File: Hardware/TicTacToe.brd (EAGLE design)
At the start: 111.7 x 101.3 mm, 37 parts, among them J1 ARDUINO_R3_SHIELD

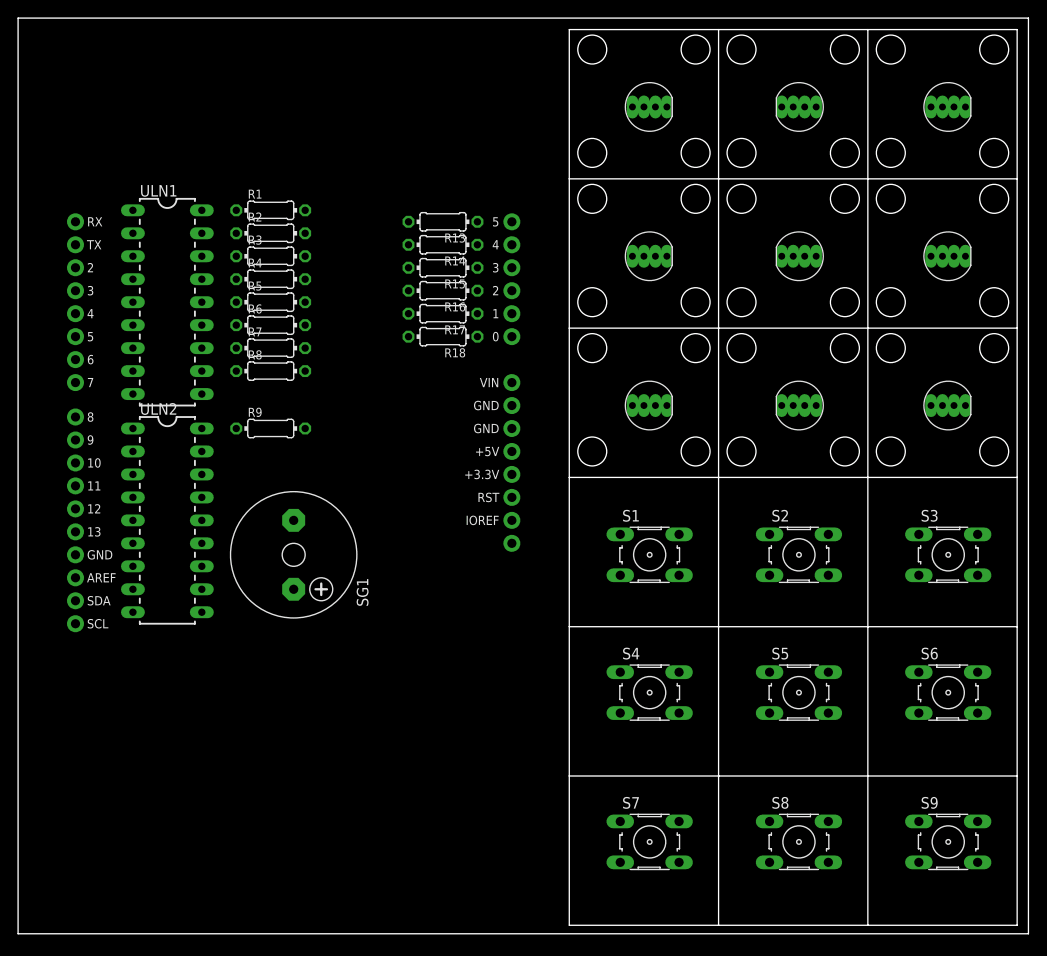
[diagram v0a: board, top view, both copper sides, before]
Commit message: Pequeño enrutado del pcb board
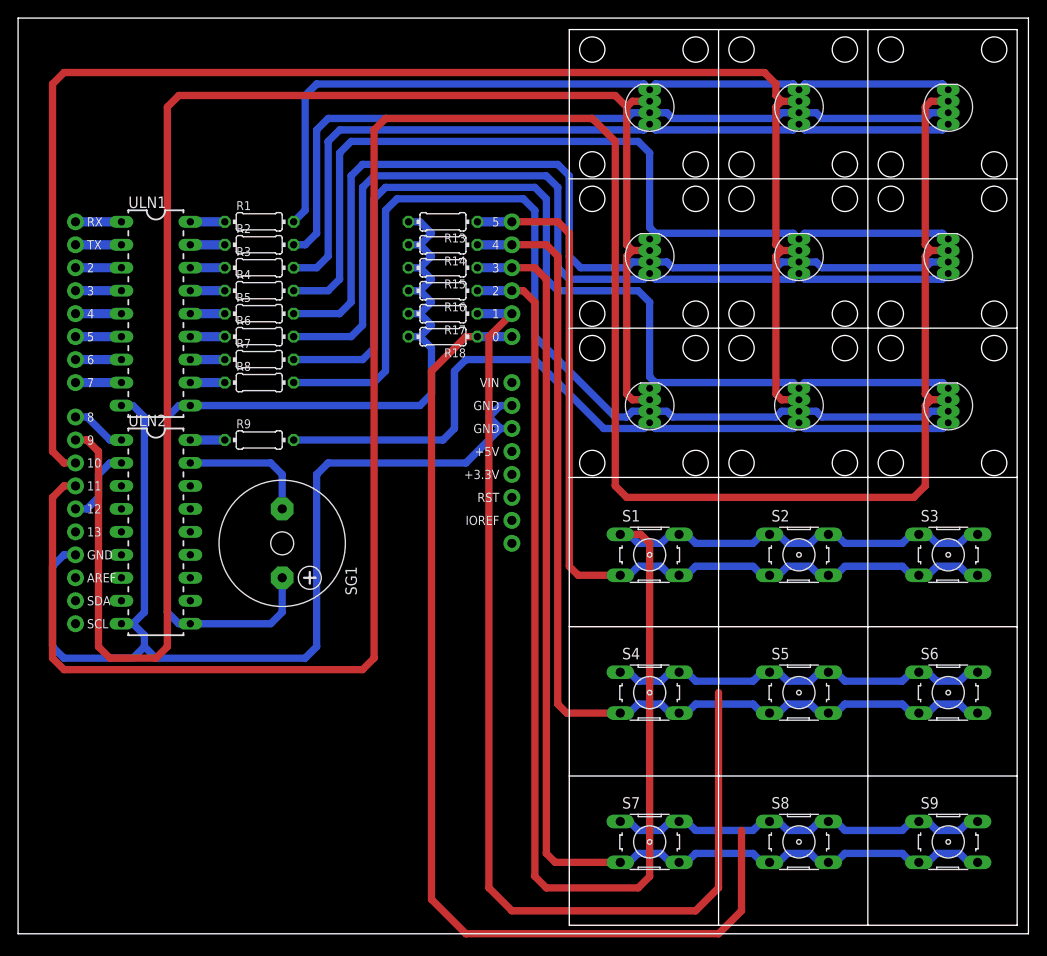
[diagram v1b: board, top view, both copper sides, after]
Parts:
- moved ULN1 1.80 mm to (41.9, 64.8)
- moved R3 1.80 mm to (53.3, 69.8)
- moved R5 1.80 mm to (53.3, 64.8)
- moved R6 1.80 mm to (53.3, 62.2)
- moved R7 1.80 mm to (53.3, 59.7)
- moved R8 1.80 mm to (53.3, 57.1)
- moved R9 1.80 mm to (53.3, 50.8)
- moved ULN2 1.80 mm to (41.9, 40.6)
- moved R1 1.80 mm to (53.3, 74.9)
- moved R2 1.80 mm to (53.3, 72.4)
- moved R4 1.80 mm to (53.3, 67.3)
- moved SG1 1.80 mm to (55.9, 39.4)
- turned D1 to 90 degrees
- turned D2 to 90 degrees
- turned D3 to 90 degrees
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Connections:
- net N$13: now also S1.4, S2.4, S3.4
- net N$18: now also S7.2, S8.2, S9.2
- net N$44: now also S4.2, S5.2, S6.2
- net N$45: now also S1.2, S2.2, S3.2
- net N$46: now also S7.4, S8.4, S9.4
- net N$47: now also S4.4, S5.4, S6.4
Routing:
- net N$43: track 0.00 -> 267.1 mm
- net N$37: track 0.00 -> 184.7 mm
- net N$45: track 0.00 -> 168.2 mm
- net N$42: track 0.00 -> 166.7 mm
- net N$44: track 0.00 -> 161.1 mm
- net N$18: track 0.00 -> 158.3 mm
- net N$46: track 0.00 -> 123.9 mm
- net GND: track 0.00 -> 121.7 mm
- net N$8: track 0.00 -> 110.7 mm
- net N$7: track 0.00 -> 110.6 mm
- net N$47: track 0.00 -> 109.9 mm
- net 5V: track 0.00 -> 101.9 mm
- net N$4: track 0.00 -> 99.9 mm
- net N$6: track 0.00 -> 98.7 mm
- net N$5: track 0.00 -> 98.1 mm
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
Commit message: Finalizacion del enrutado, solo falta reparar la libreria del RGB por overloap
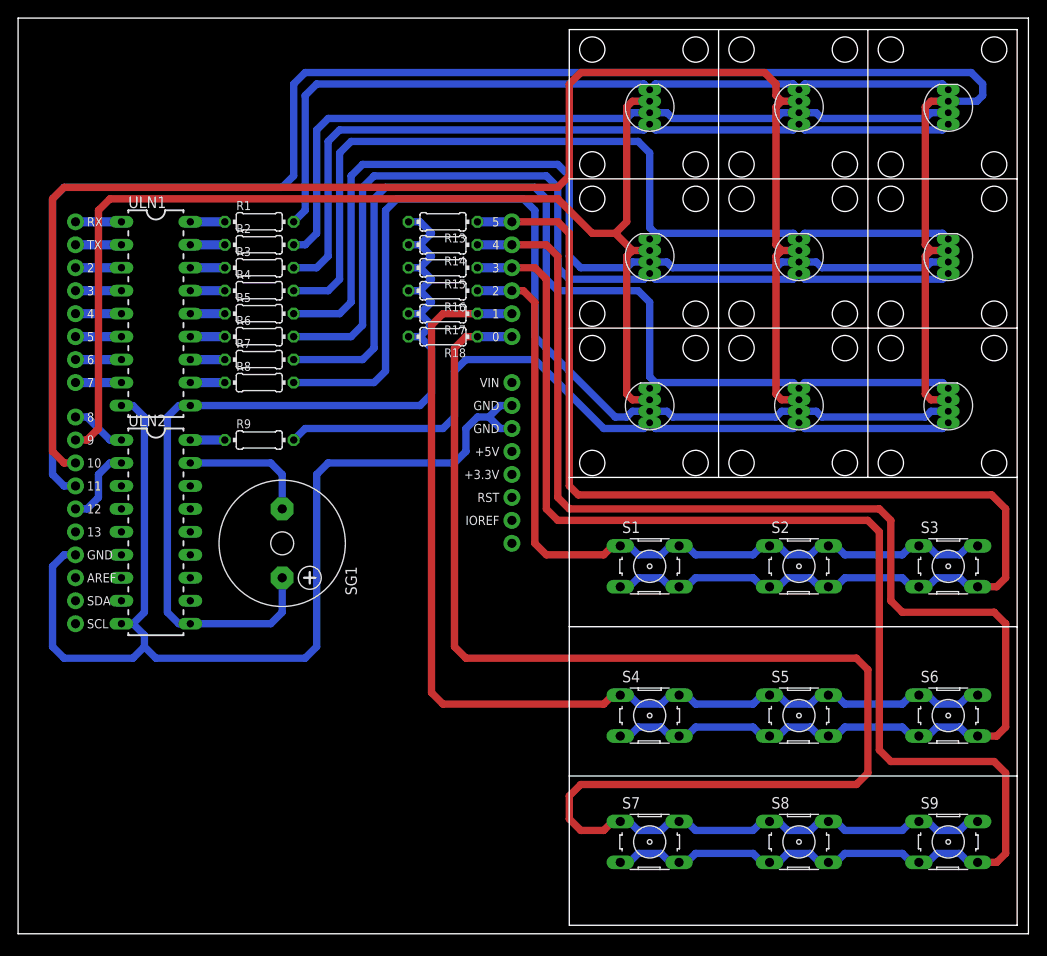
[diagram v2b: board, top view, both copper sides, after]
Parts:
- moved S4 2.54 mm to (96.5, 20.3)
- moved S5 2.54 mm to (113.0, 20.3)
- moved S6 2.54 mm to (129.5, 20.3)
- moved S1 1.27 mm to (96.5, 36.8)
- moved S2 1.27 mm to (113.0, 36.8)
- moved S3 1.27 mm to (129.5, 36.8)
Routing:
- net N$45: track 168.2 -> 87.6 mm
- net N$43: track 267.1 -> 193.8 mm
- net N$37: track 184.7 -> 127.3 mm
- net N$44: track 161.1 -> 115.5 mm
- net N$13: track 97.2 -> 142.7 mm
- net N$47: track 109.9 -> 155.2 mm
- net N$46: track 123.9 -> 166.6 mm
- net N$18: track 158.3 -> 184.9 mm
- net N$42: track 166.7 -> 165.2 mm
- net GND: track 121.7 -> 122.4 mm
- net N$9: track 84.3 -> 83.5 mm
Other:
- outline, holes or cut-outs redrawn
